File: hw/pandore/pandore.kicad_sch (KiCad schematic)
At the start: 21 parts

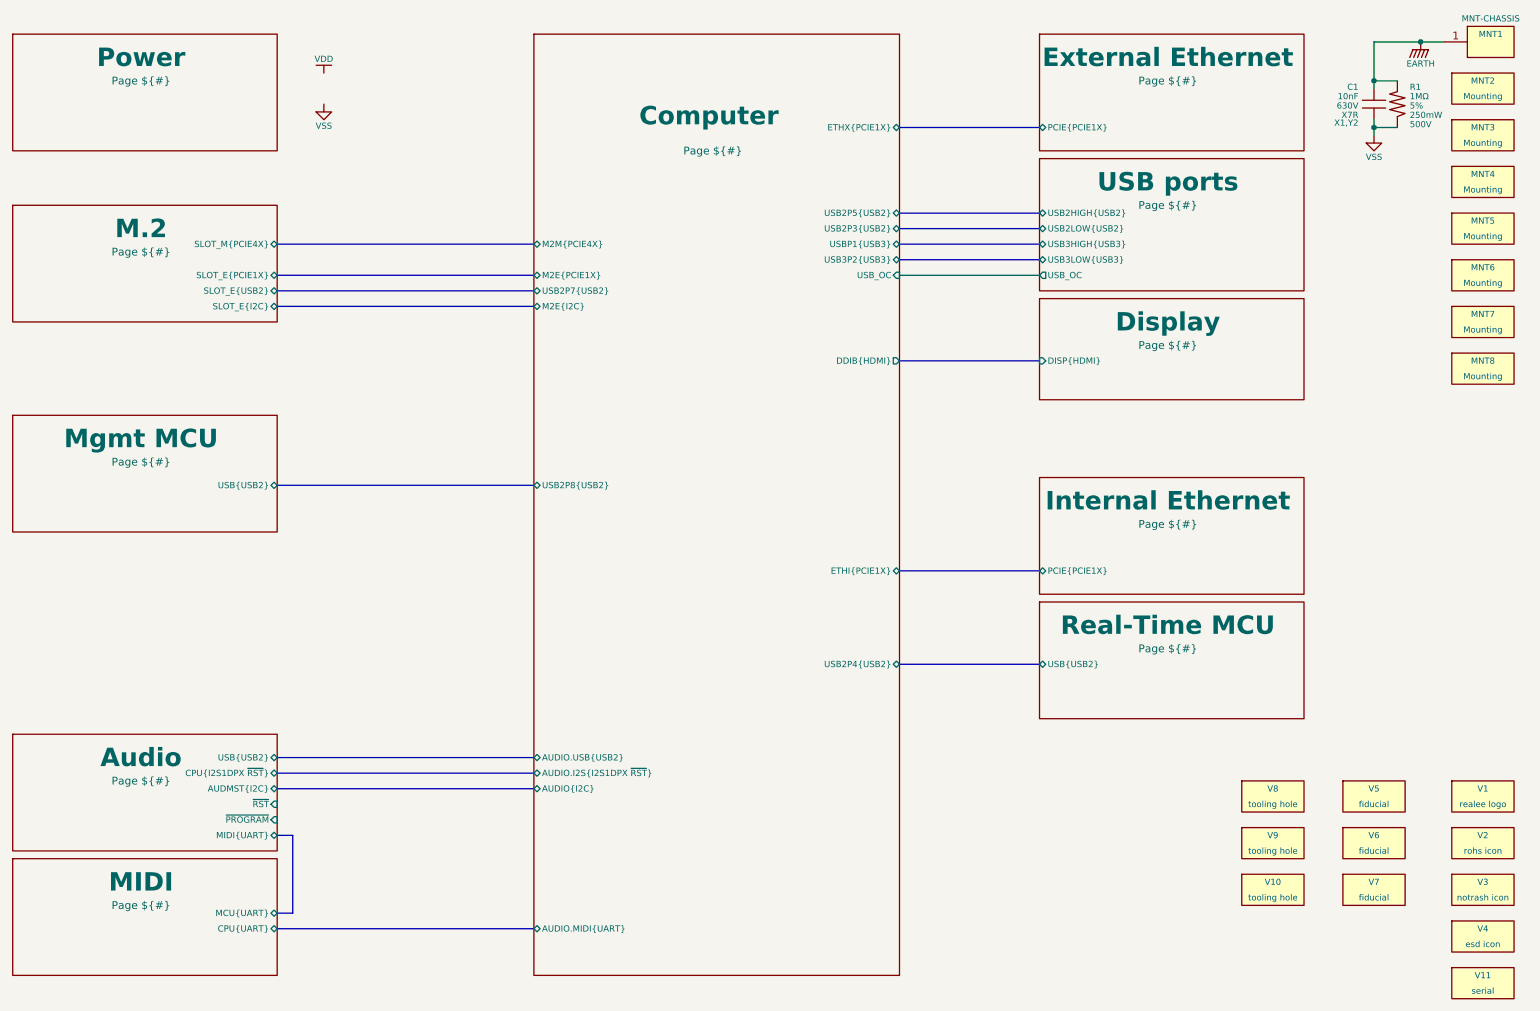
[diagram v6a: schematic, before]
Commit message: most of board control signals added, routed and defined
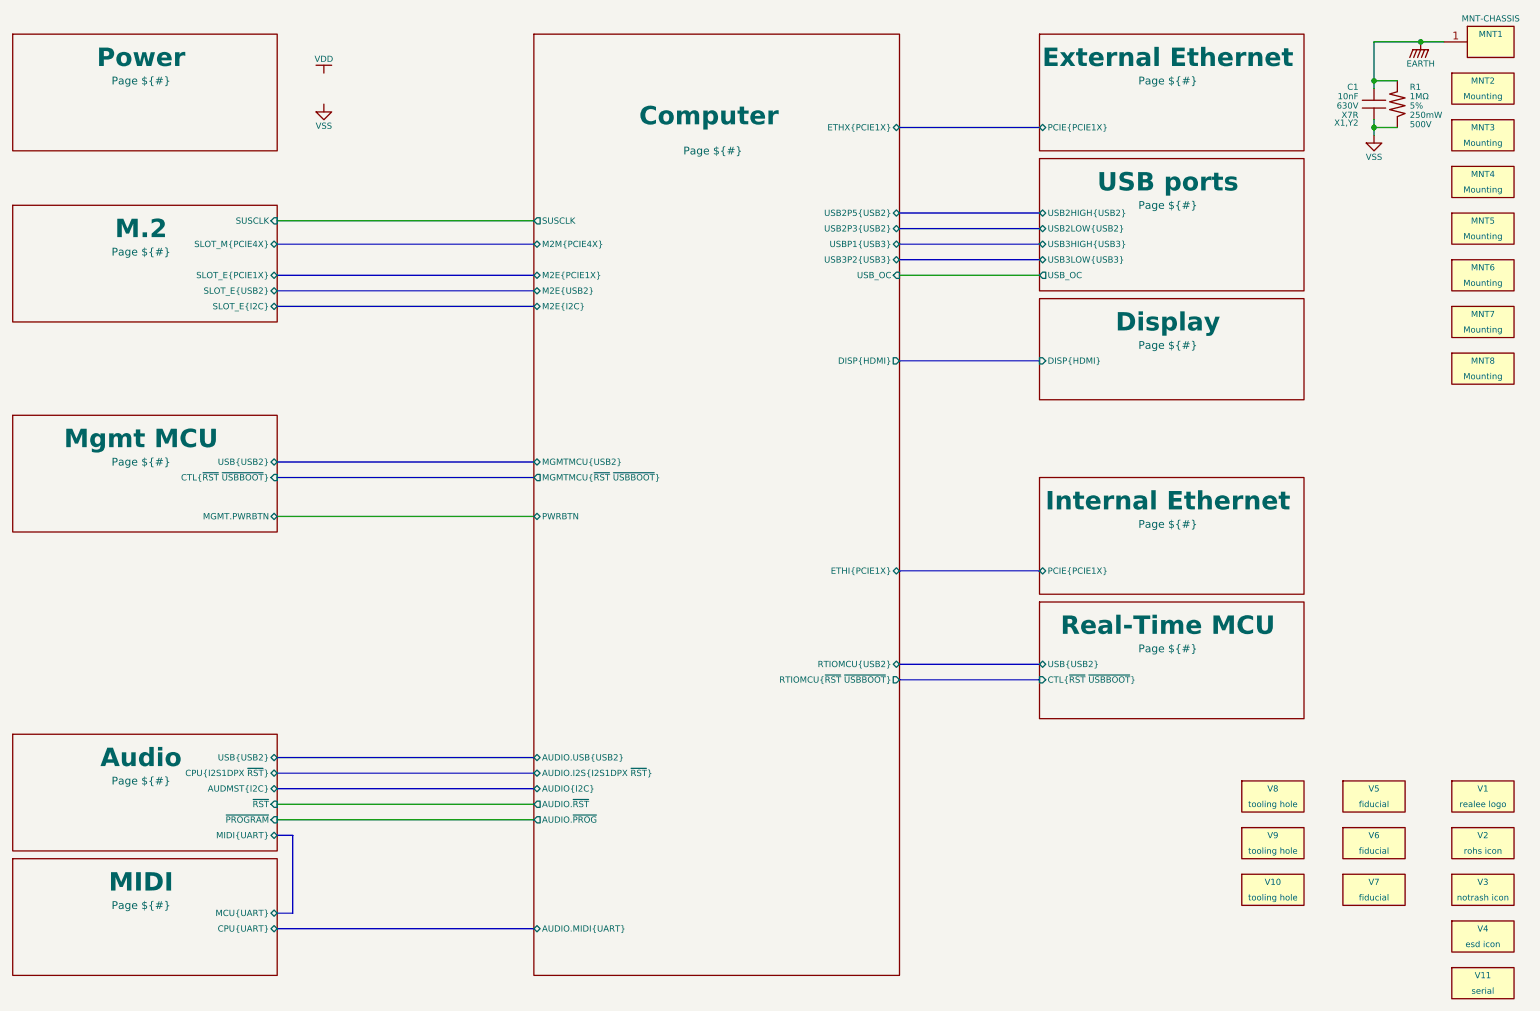
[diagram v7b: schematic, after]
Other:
- sheet Computer ports: added AUDIO.~{PROG}, AUDIO.~{RST}, DISP{HDMI}, M2E{USB2}, MGMTMCU{USB2}, MGMTMCU{~{RST} ~{USBBOOT}}, PWRBTN, RTIOMCU{USB2}, RTIOMCU{~{RST} ~{USBBOOT}}, SUSCLK; removed DDIB{HDMI}, USB2P4{USB2}, USB2P7{USB2}, USB2P8{USB2}
- sheet M.2 ports: added SUSCLK; removed none
- sheet Mgmt MCU ports: added CTL{~{RST} ~{USBBOOT}}, MGMT.PWRBTN; removed none
- sheet Real-Time MCU ports: added CTL{~{RST} ~{USBBOOT}}; removed none
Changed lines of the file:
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@@
 	(bus
 		(pts
-			(xy 76.2 92.71) (xy 118.11 92.71)
+			(xy 76.2 88.9) (xy 118.11 88.9)
 		)
 		(stroke
@@
 	(bus
 		(pts
+			(xy 177.8 124.46) (xy 200.66 124.46)
+		)
+		(stroke
+			(width 0)
+			(type default)
+		)
+	)
+	(bus
+		(pts
 			(xy 177.8 50.8) (xy 200.66 50.8)
 		)
@@
 		)
 	)
+	(wire
+		(pts
+			(xy 76.2 144.78) (xy 118.11 144.78)
+		)
+		(stroke
+			(width 0)
+			(type default)
+		)
+	)
 	(bus
 		(pts
@@
 		)
 	)
+	(wire
+		(pts
+			(xy 76.2 97.79) (xy 118.11 97.79)
+		)
+		(stroke
+			(width 0)
+			(type default)
+		)
+	)
 	(bus
 		(pts
@@
 		)
 	)
+	(wire
+		(pts
+			(xy 76.2 147.32) (xy 118.11 147.32)
+		)
+		(stroke
+			(width 0)
+			(type default)
+		)
+	)
 	(bus
 		(pts
@@
 	(wire
 		(pts
+			(xy 76.2 49.53) (xy 118.11 49.53)
+		)
+		(stroke
+			(width 0)
+			(type default)
+		)
+	)
+	(bus
+		(pts
+			(xy 76.2 91.44) (xy 118.11 91.44)
+		)
+		(stroke
+			(width 0)
+			(type default)
+		)
+	)
+	(wire
+		(pts
 			(xy 255.27 33.02) (xy 255.27 34.29)
 		)
@@
 		)
 		(pin "USB{USB2}" bidirectional
-			(at 76.2 92.71 0)
+			(at 76.2 88.9 0)
+			(effects
+				(font
+					(size 1.016 1.016)
+				)
+				(justify right)
+			)
+		)
+		(pin "CTL{~{RST} ~{USBBOOT}}" input
+			(at 76.2 91.44 0)
+			(effects
+				(font
+					(size 1.016 1.016)
+				)
+				(justify right)
+			)
+		)
+		(pin "MGMT.PWRBTN" bidirectional
+			(at 76.2 97.79 0)
 			(effects
 				(font
@@
 			)
 		)
-		(pin "USB2P8{USB2}" bidirectional
-			(at 118.11 92.71 180)
-			(effects
-				(font
-					(size 1.016 1.016)
-				)
-				(justify left)
-			)
-		)
-		(pin "USB2P7{USB2}" bidirectional
-			(at 118.11 60.96 180)
-			(effects
-				(font
-					(size 1.016 1.016)
-				)
-				(justify left)
-			)
-		)
 		(pin "USB2P3{USB2}" bidirectional
 			(at 177.8 50.8 0)
@@
 			)
 		)
-		(pin "DDIB{HDMI}" output
-			(at 177.8 72.39 0)
-			(effects
-				(font
-					(size 1.016 1.016)
-				)
-				(justify right)
-			)
-		)
-		(pin "USB2P4{USB2}" bidirectional
-			(at 177.8 121.92 0)
-			(effects
-				(font
-					(size 1.016 1.016)
-				)
-				(justify right)
-			)
-		)
 		(pin "USBP1{USB3}" bidirectional
 			(at 177.8 53.34 0)
@@
 			)
 		)
+		(pin "AUDIO.~{PROG}" output
+			(at 118.11 147.32 180)
+			(effects
+				(font
+					(size 1.016 1.016)
+				)
+				(justify left)
+			)
+		)
+		(pin "AUDIO.~{RST}" output
+			(at 118.11 144.78 180)
+			(effects
+				(font
+					(size 1.016 1.016)
+				)
+				(justify left)
+			)
+		)
+		(pin "SUSCLK" output
+			(at 118.11 49.53 180)
+			(effects
+				(font
+					(size 1.016 1.016)
+				)
+				(justify left)
+			)
+		)
+		(pin "MGMTMCU{USB2}" bidirectional
+			(at 118.11 88.9 180)
+			(effects
+				(font
+					(size 1.016 1.016)
+				)
+				(justify left)
+			)
+		)
+		(pin "RTIOMCU{USB2}" bidirectional
+			(at 177.8 121.92 0)
+			(effects
+				(font
+					(size 1.016 1.016)
+				)
+				(justify right)
+			)
+		)
+		(pin "DISP{HDMI}" output
+			(at 177.8 72.39 0)
+			(effects
+				(font
+					(size 1.016 1.016)
+				)
+				(justify right)
+			)
+		)
+		(pin "M2E{USB2}" bidirectional
+			(at 118.11 60.96 180)
+			(effects
+				(font
+					(size 1.016 1.016)
+				)
+				(justify left)
+			)
+		)
+		(pin "RTIOMCU{~{RST} ~{USBBOOT}}" output
+			(at 177.8 124.46 0)
+			(effects
+				(font
+					(size 1.016 1.016)
+				)
+				(justify right)
+			)
+		)
+		(pin "MGMTMCU{~{RST} ~{USBBOOT}}" output
+			(at 118.11 91.44 180)
+			(effects
+				(font
+					(size 1.016 1.016)
+				)
+				(justify left)
+			)
+		)
+		(pin "PWRBTN" bidirectional
+			(at 118.11 97.79 180)
+			(effects
+				(font
+					(size 1.016 1.016)
+				)
+				(justify left)
+			)
+		)
 		(instances
 			(project "pandore"
@@
 			)
 		)
+		(pin "SUSCLK" input
+			(at 76.2 49.53 0)
+			(effects
+				(font
+					(size 1.016 1.016)
+				)
+				(justify right)
+			)
+		)
 		(instances
 			(project "pandore"
@@
 			(effects
 				(font
+					(size 1.016 1.016)
+				)
+				(justify left)
+			)
+		)
+		(pin "CTL{~{RST} ~{USBBOOT}}" input
+			(at 200.66 124.46 180)
+			(effects
+				(font

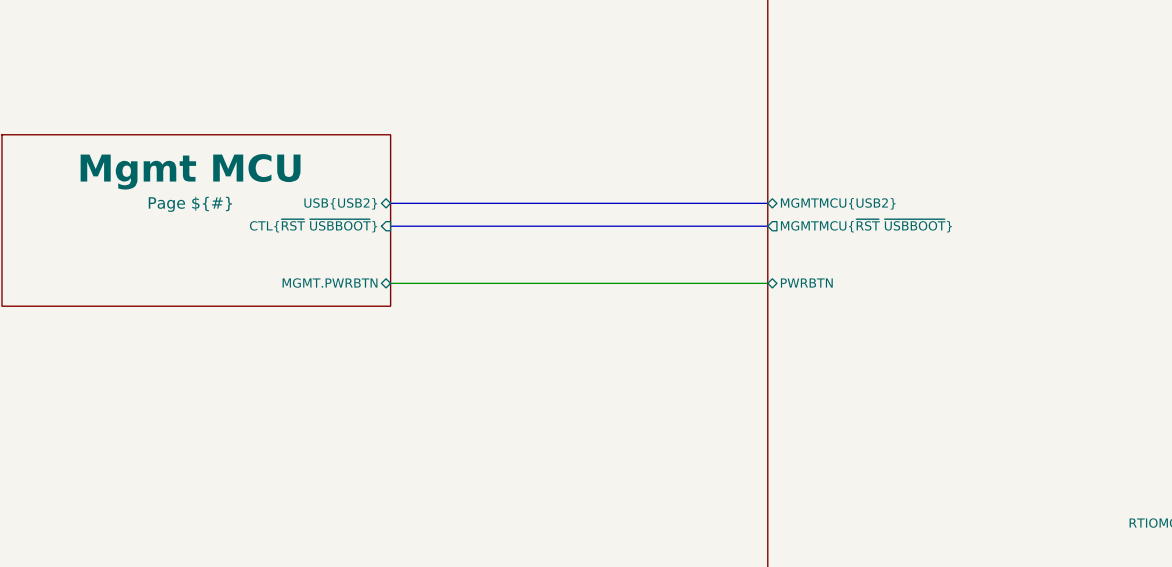
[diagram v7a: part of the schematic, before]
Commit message: added expansion port and more ctl to rp2350s routing much progress
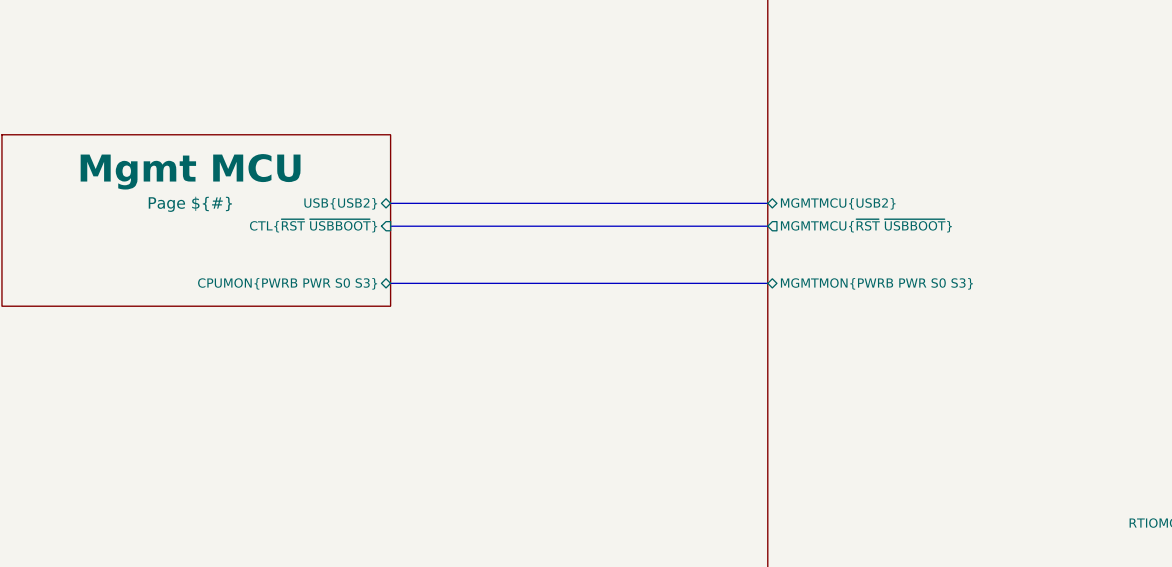
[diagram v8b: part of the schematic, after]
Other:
- sheet Computer ports: added MGMTMON{PWRB PWR S0 S3}; removed PWRBTN
- sheet Mgmt MCU ports: added CPUMON{PWRB PWR S0 S3}; removed MGMT.PWRBTN
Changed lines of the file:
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@@
 		)
 	)
+	(bus
+		(pts
+			(xy 76.2 97.79) (xy 118.11 97.79)
+		)
+		(stroke
+			(width 0)
+			(type default)
+		)
+	)
 	(wire
 		(pts
@@
 		)
 	)
-	(wire
-		(pts
-			(xy 76.2 97.79) (xy 118.11 97.79)
-		)
-		(stroke
-			(width 0)
-			(type default)
-		)
-	)
 	(bus
 		(pts
@@
 			)
 		)
-		(pin "MGMT.PWRBTN" bidirectional
+		(pin "CPUMON{PWRB PWR S0 S3}" bidirectional
 			(at 76.2 97.79 0)
 			(effects
@@
 			)
 		)
-		(pin "PWRBTN" bidirectional
+		(pin "MGMTMON{PWRB PWR S0 S3}" bidirectional
 			(at 118.11 97.79 180)
 			(effects
